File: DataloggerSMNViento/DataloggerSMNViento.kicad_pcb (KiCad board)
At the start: 2 copper layers, 85.7 x 137.2 mm, 46 parts, among them J1 Screw_Terminal_01x03, J2 Screw_Terminal_01x02, J3 Vcc 5V SD, J4 GND SD, Q1 Q_NPN_BEC, Q2 Q_NPN_BEC, Q3 Q_NPN_BEC, Q4 Q_NPN_BEC, U1 MAX485E, U2 w5100_module, U3 LM2596S-HW-319-v6_module, U5 LM358

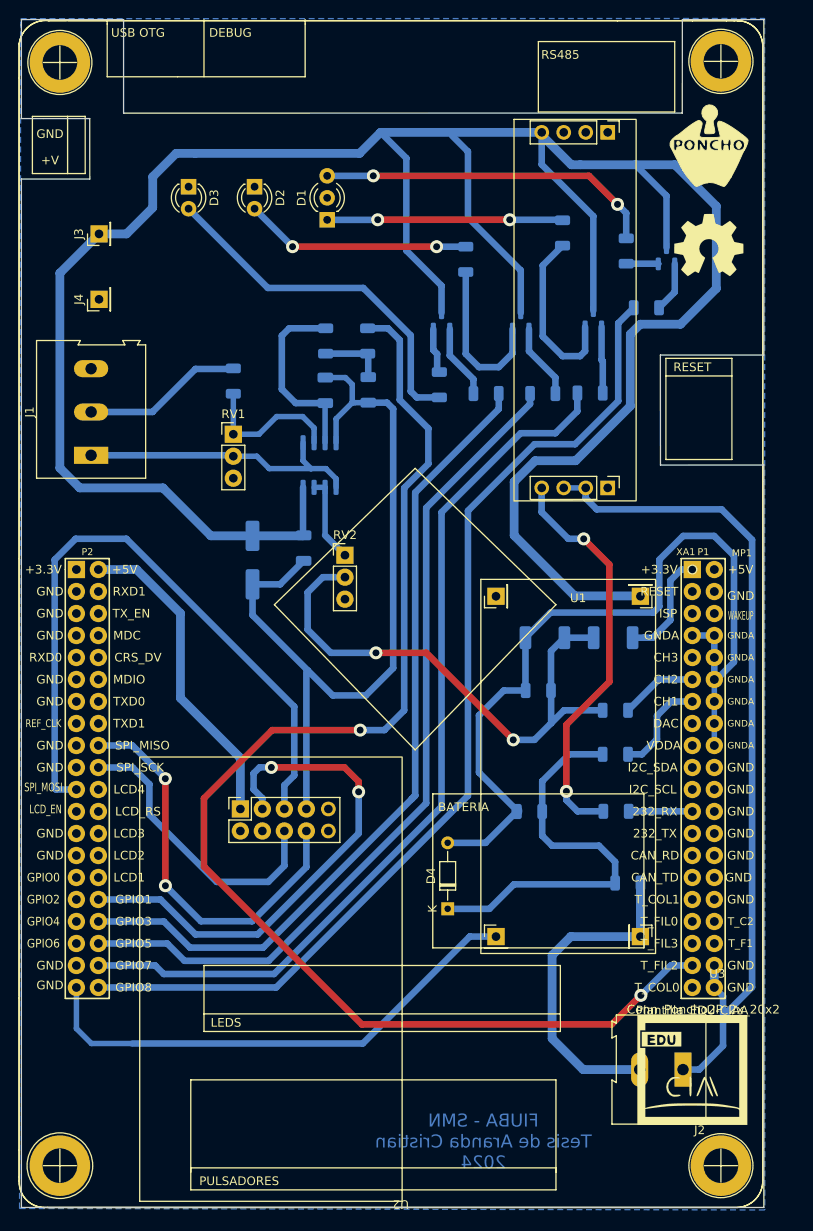
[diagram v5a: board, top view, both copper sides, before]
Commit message: Se debe cambiar el diseño porque el footprint del  StepDown esta invertido, lo cual va a implicar cambiar algunas pistas
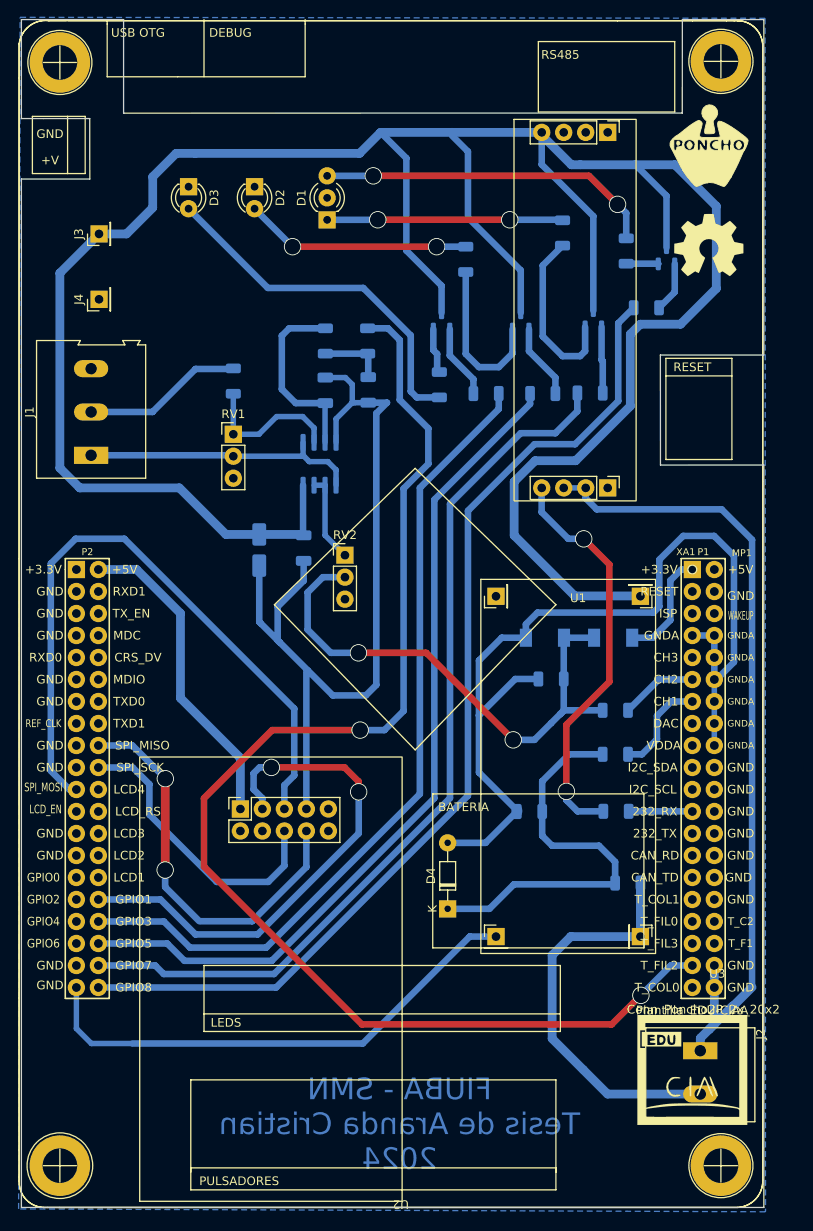
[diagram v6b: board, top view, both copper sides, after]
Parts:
- C4: footprint Capacitor_SMD:CP_Elec_6.3x9.9 -> Capacitor_SMD:CP_Elec_4x5.3
- D5, D6: footprint Diode_SMD:D_2010_5025Metric -> Diode_SMD:D_SOD-128
- U5: footprint Package_SO:SO-8_3.9x4.9mm_P1.27mm -> Package_SO:SOIC-8_3.9x4.9mm_P1.27mm
- moved J2 2.95 mm to (152.1, 144.5), turned to -90 degrees
- moved R15 1.98 mm to (134.8, 101.5)
- moved C4 1.40 mm to (101.1, 86.7)
- moved U5 0.14 mm to (108.1, 76.7)
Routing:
- net GNDA: track 98.7 -> 108.4 mm
- net +12V: track 38.5 -> 46.7 mm
- net GNDinVariador: track 268.3 -> 270.5 mm
- net ADCinVariador: track 33.8 -> 32.3 mm
- net Net-(D5-Pad2): track 64.0 -> 62.6 mm
- net /Conector del Poncho/MOSI: track 77.9 -> 77.3 mm
